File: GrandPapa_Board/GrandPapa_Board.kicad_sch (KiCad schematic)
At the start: 5 parts, among them J1 Conn_01x03_Female, J2 Conn_02x06, J3 M80-5000642, J4 M80-5000642, J5 M80-5000642

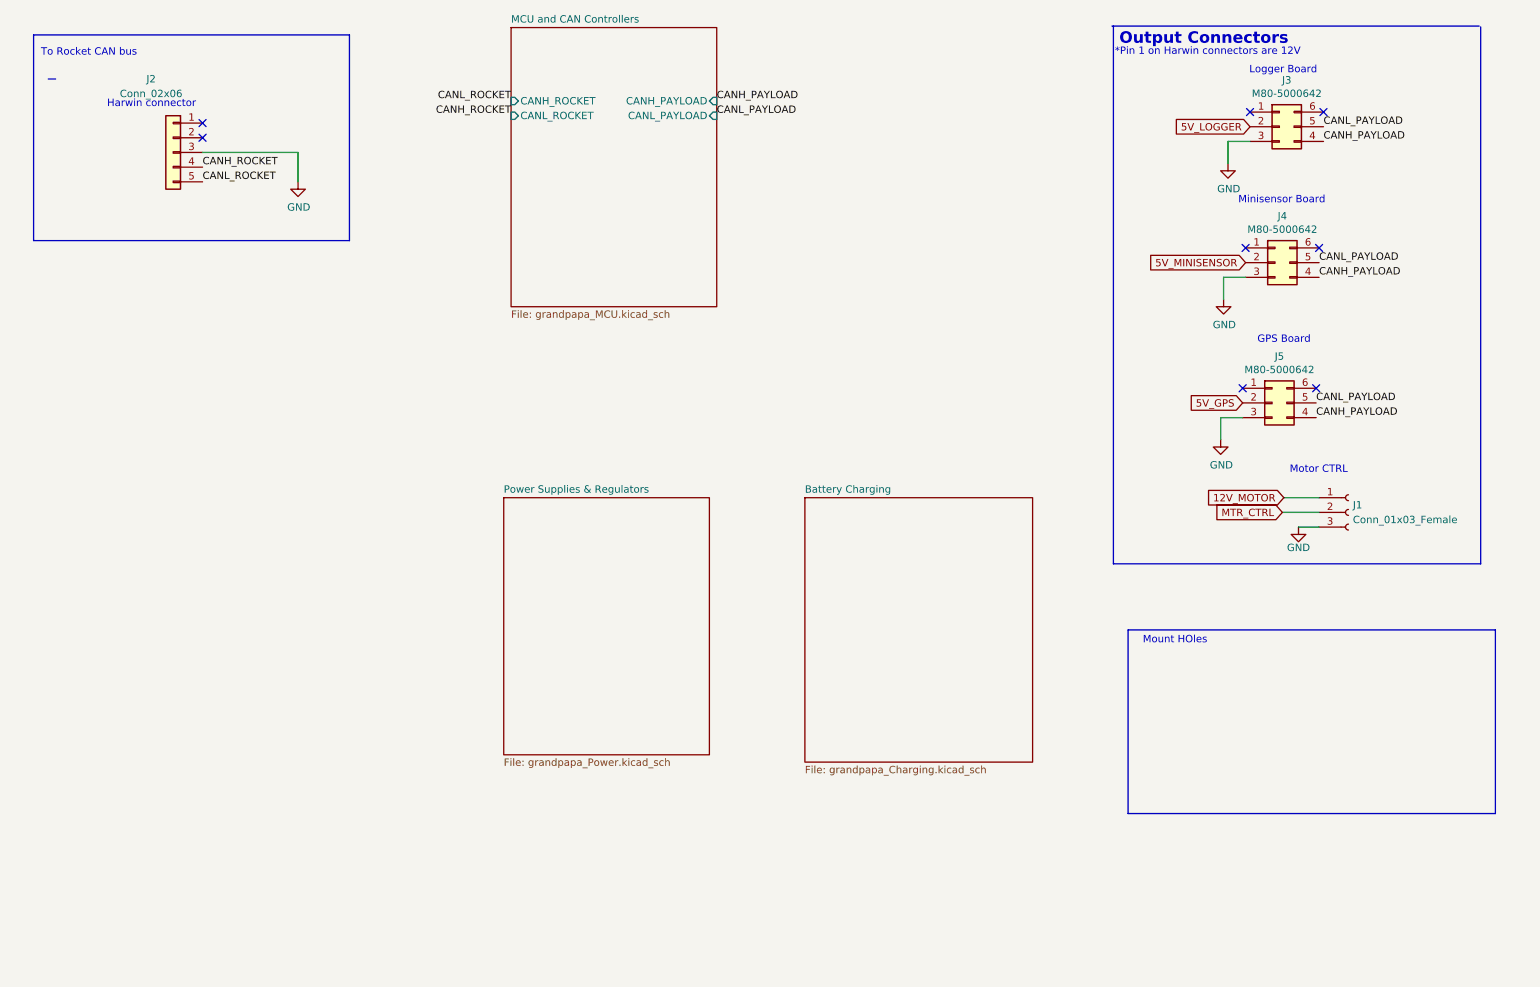
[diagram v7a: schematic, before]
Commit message: clean up schematic, edit nets for clarification, add gnd test points, edit load switching scheme
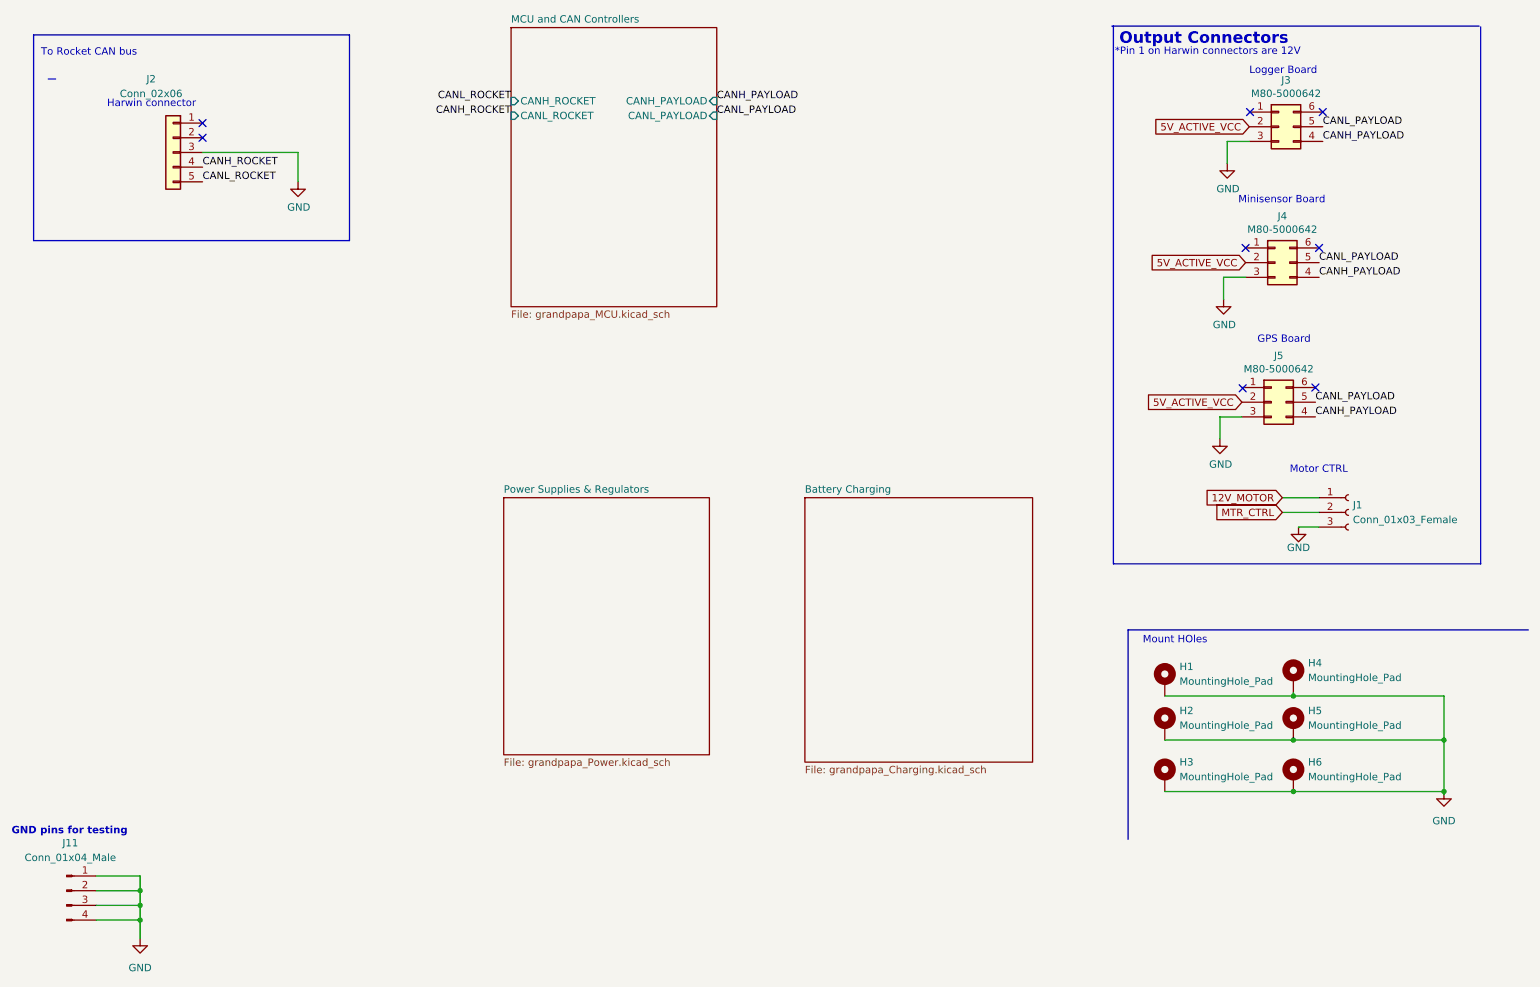
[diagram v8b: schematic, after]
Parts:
- added H1, H2, H3, H4, H5, H6: MountingHole_Pad, symbol Mechanical:MountingHole_Pad
- added J11: Conn_01x04_Male, symbol Connector:Conn_01x04_Male
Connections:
- net 5V_LOGGER is gone; now on net 5V_ACTIVE_VCC: J3.2 (Pin_2)
- net 5V_MINISENSOR is gone; now on net 5V_ACTIVE_VCC: J4.2 (Pin_2)
- net GND: now also H1.1, H2.1, H3.1, H4.1, H5.1, H6.1, J11.1 (Pin_1), J11.2 (Pin_2), J11.3 (Pin_3), J11.4 (Pin_4)
- net 5V_GPS renamed 5V_ACTIVE_VCC
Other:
- note added: "GND pins for testing"
